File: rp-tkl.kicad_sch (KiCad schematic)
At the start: 35 parts, among them J1 USB_C_Receptacle_USB2.0, J2 SWD, J3 Conn_01x04_Female, J4 Conn_01x06_Female, SW0 SW_Push, U1 XC6206PxxxMR, U2 RP2040, U3 SRV05-4, U4 W25Q128JVS, Y1 12MHz

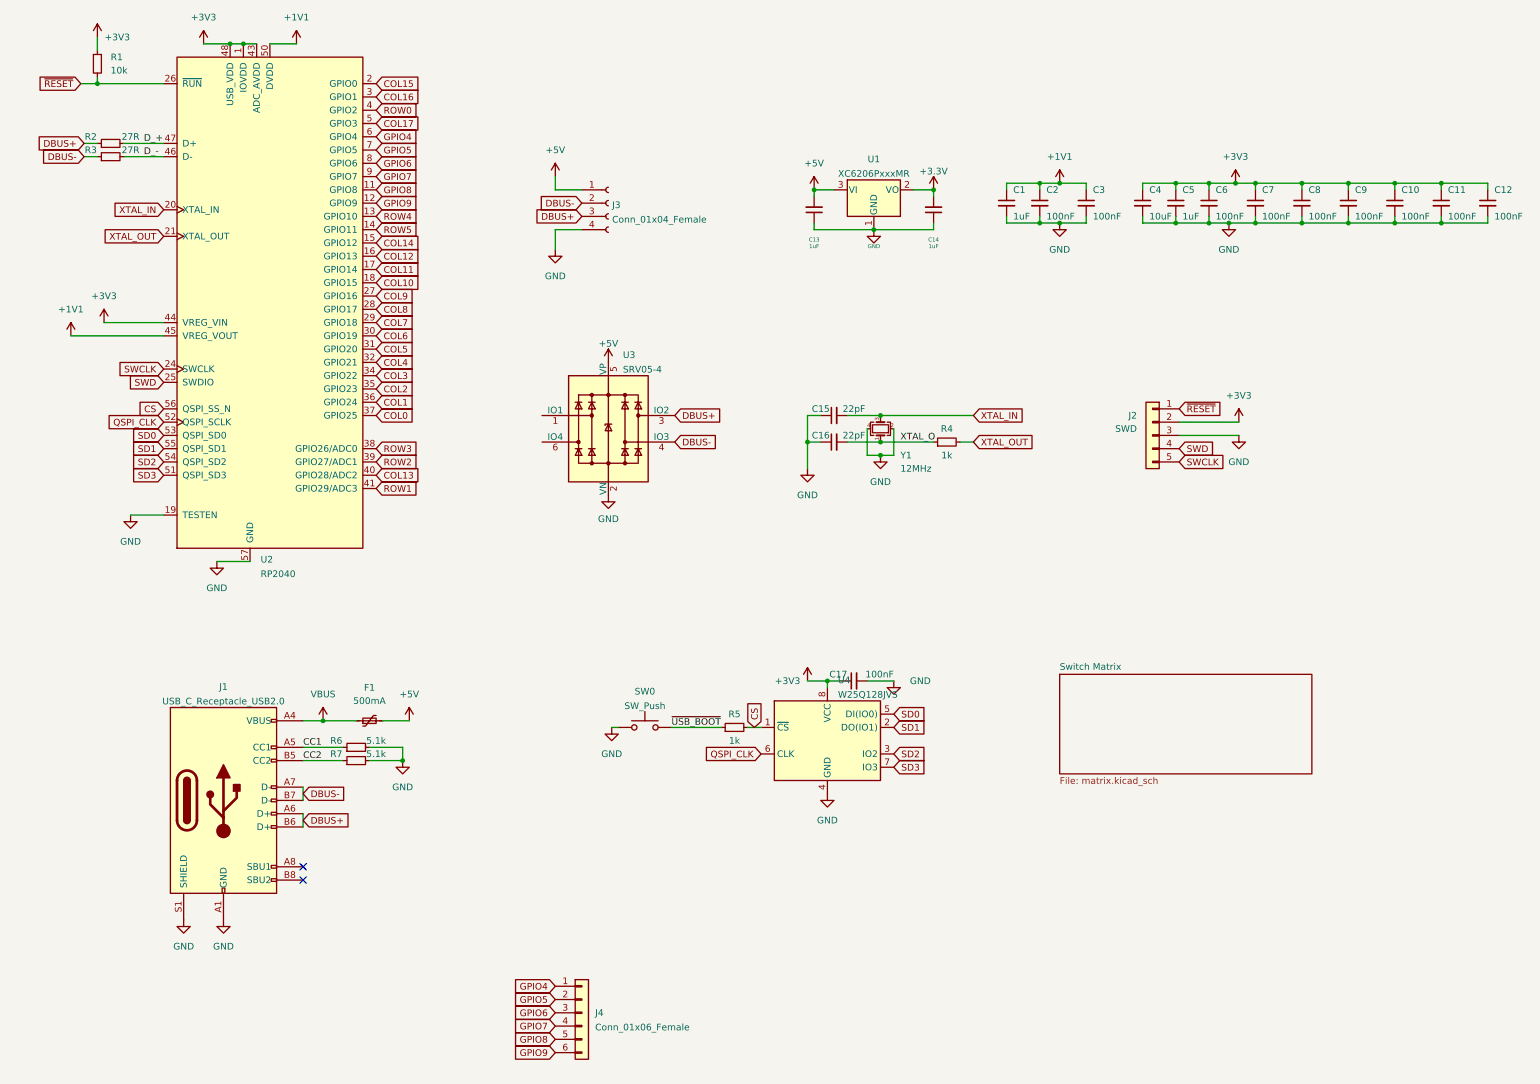
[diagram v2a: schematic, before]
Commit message: Cleaned up silkscreen and fab layers
Also adjusted some of the component descriptions/names
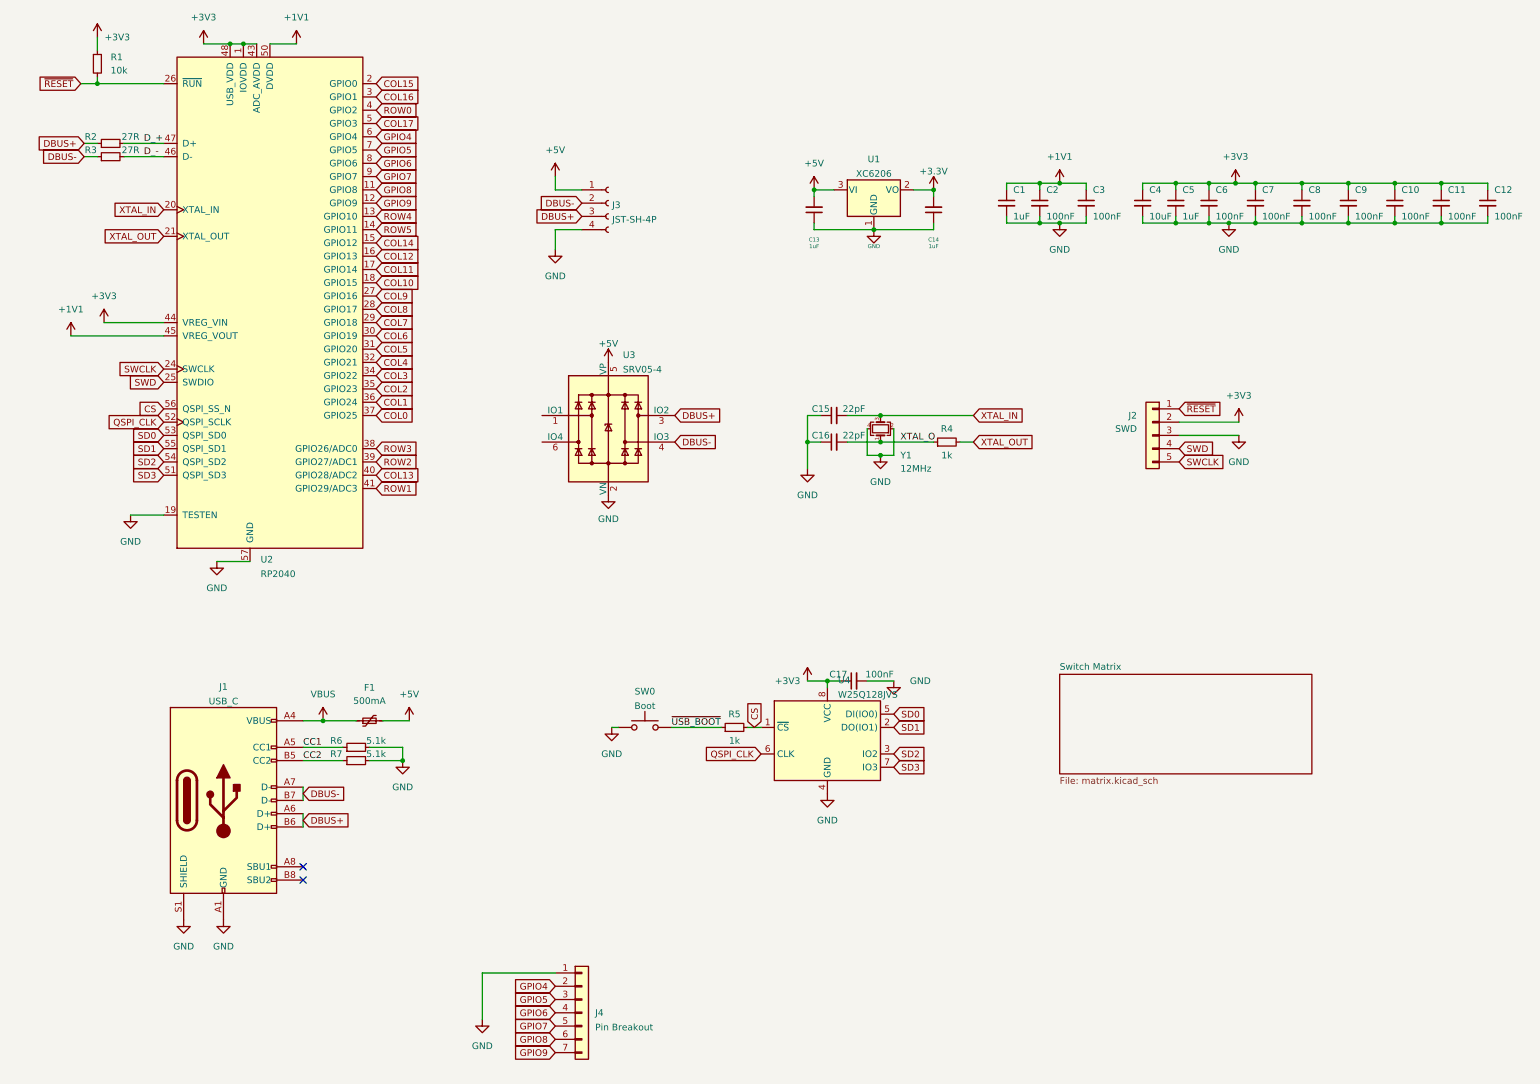
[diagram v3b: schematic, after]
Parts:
- J1: value USB_C_Receptacle_USB2.0 -> USB_C
- J3: value Conn_01x04_Female -> JST-SH-4P
- J4: value Conn_01x06_Female -> Pin Breakout; footprint Connector_PinSocket_2.54mm:PinSocket_1x06_P2.54mm_Vertical -> Connector_PinSocket_2.54mm:PinSocket_1x07_P2.54mm_Vertical; symbol Connector_Generic:Conn_01x06 -> Connector_Generic:Conn_01x07
- SW0: value SW_Push -> Boot
- U1: value XC6206PxxxMR -> XC6206
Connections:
- net GND: now also J4.1 (Pin_1)
- net GPIO4: now also J4.2 (Pin_2); no longer J4.1 (Pin_1)
- net GPIO5: now also J4.3 (Pin_3); no longer J4.2 (Pin_2)
- net GPIO6: now also J4.4 (Pin_4); no longer J4.3 (Pin_3)
- net GPIO7: now also J4.5 (Pin_5); no longer J4.4 (Pin_4)
- net GPIO8: now also J4.6 (Pin_6); no longer J4.5 (Pin_5)
- net GPIO9: now also J4.7 (Pin_7); no longer J4.6 (Pin_6)
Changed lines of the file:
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@@
+    (stroke (width 0) (type default) (color 0 0 0 0))
+  )
+  (wire (pts (xy 120.65 219.71) (xy 106.68 219.71))
     (stroke (width 0) (type default) (color 0 0 0 0))
   )
@@
   )
   (wire (pts (xy 207.01 68.58) (xy 207.01 69.85))
+    (stroke (width 0) (type default) (color 0 0 0 0))
+  )
+  (wire (pts (xy 106.68 219.71) (xy 106.68 228.6))
     (stroke (width 0) (type default) (color 0 0 0 0))
   )
@@
     (in_bom yes) (on_board yes) (fields_autoplaced)
     (property "Reference" "U1" (id 0) (at 181.61 63.9785 0))
-    (property "Value" "XC6206PxxxMR" (id 1) (at 181.61 66.7536 0))
+    (property "Value" "XC6206" (id 1) (at 181.61 66.7536 0))
     (property "Footprint" "Package_TO_SOT_SMD:SOT-23" (id 2) (at 181.61 64.135 0)
       (effects (font (size 1.27 1.27) italic) hide)
@@
     (pin "1")
   )
-  (symbol (lib_id "Connector_Generic:Conn_01x06") (at 125.73 227.33 0) (unit 1)
+  (symbol (lib_id "Connector_Generic:Conn_01x07") (at 125.73 227.33 0) (unit 1)
     (in_bom yes) (on_board yes)
     (property "Reference" "J4" (id 0) (at 128.27 227.33 0)
       (effects (font (size 1.27 1.27)) (justify left))
     )
-    (property "Value" "Conn_01x06_Female" (id 1) (at 128.27 230.1051 0)
-      (effects (font (size 1.27 1.27)) (justify left))
-    )
-    (property "Footprint" "Connector_PinSocket_2.54mm:PinSocket_1x06_P2.54mm_Vertical" (id 2) (at 125.73 227.33 0)
+    (property "Value" "Pin Breakout" (id 1) (at 128.27 230.1051 0)
+      (effects (font (size 1.27 1.27)) (justify left))
+    )
+    (property "Footprint" "Connector_PinSocket_2.54mm:PinSocket_1x07_P2.54mm_Vertical" (id 2) (at 125.73 227.33 0)
       (effects (font (size 1.27 1.27)) hide)
     )
@@
     (pin "5")
     (pin "6")
+    (pin "7")
   )
   (symbol (lib_id "Device:Crystal_GND24_Small") (at 182.88 115.57 90) (unit 1)
@@
     (in_bom yes) (on_board yes) (fields_autoplaced)
     (property "Reference" "J1" (id 0) (at 57.15 164.9435 0))
-    (property "Value" "USB_C_Receptacle_USB2.0" (id 1) (at 57.15 167.7186 0))
+    (property "Value" "USB_C" (id 1) (at 57.15 167.7186 0))
     (property "Footprint" "Connector_USB:USB_C_Receptacle_HRO_TYPE-C-31-M-12" (id 2) (at 60.96 186.69 0)
       (effects (font (size 1.27 1.27)) hide)
@@
     (pin "2")
   )
+  (symbol (lib_id "power:GND") (at 106.68 228.6 0) (unit 1)
+    (in_bom yes) (on_board yes) (fields_autoplaced)
+    (property "Reference" "#PWR0104" (id 0) (at 106.68 234.95 0)
+      (effects (font (size 1.27 1.27)) hide)
+    )
+    (property "Value" "GND" (id 1) (at 106.68 233.68 0))
+    (property "Footprint" "" (id 2) (at 106.68 228.6 0)
+      (effects (font (size 1.27 1.27)) hide)
+    )
+    (property "Datasheet" "" (id 3) (at 106.68 228.6 0)
+      (effects (font (size 1.27 1.27)) hide)
+    )
+    (pin "1")
+  )
   (symbol (lib_id "power:+5V") (at 92.71 171.45 0) (unit 1)
     (in_bom yes) (on_board yes) (fields_autoplaced)
@@
       (effects (font (size 1.27 1.27)) (justify left))
     )
-    (property "Value" "Conn_01x04_Female" (id 1) (at 131.5212 75.5266 0)
+    (property "Value" "JST-SH-4P" (id 1) (at 131.5212 75.5266 0)
       (effects (font (size 1.27 1.27)) (justify left))
     )
@@
     (in_bom no) (on_board yes) (fields_autoplaced)
     (property "Reference" "SW0" (id 0) (at 137.795 165.8325 0))
-    (property "Value" "SW_Push" (id 1) (at 137.795 168.6076 0))
+    (property "Value" "Boot" (id 1) (at 137.795 168.6076 0))
     (property "Footprint" "Connector_PinSocket_2.54mm:PinSocket_1x02_P2.54mm_Vertical" (id 2) (at 137.795 167.64 0)
       (effects (font (size 1.27 1.27)) hide)
@@
       (reference "#PWR0103") (unit 1) (value "+5V") (footprint "")
     )
+    (path "/87e21c8d-439e-4759-a401-59d374da92eb"
+      (reference "#PWR0104") (unit 1) (value "GND") (footprint "")
+    )
     (path "/29f11a32-f398-46d6-95a0-57f3be58392e"
       (reference "C1") (unit 1) (value "1uF") (footprint "Capacitor_SMD:C_0402_1005Metric")
@@
     )
     (path "/7ebbe95b-f237-4c94-ae3b-fbe07dfc9bfc"
-      (reference "J1") (unit 1) (value "USB_C_Receptacle_USB2.0") (footprint "Connector_USB:USB_C_Receptacle_HRO_TYPE-C-31-M-12")
+      (reference "J1") (unit 1) (value "USB_C") (footprint "Connector_USB:USB_C_Receptacle_HRO_TYPE-C-31-M-12")
     )
     (path "/488e1dfc-da13-4e5c-9edf-756b09e35c04"
@@
     )
     (path "/cd299587-3566-48c2-b7b0-ede206393480"
-      (reference "J3") (unit 1) (value "Conn_01x04_Female") (footprint "Connector_JST:JST_SH_SM04B-SRSS-TB_1x04-1MP_P1.00mm_Horizontal")
+      (reference "J3") (unit 1) (value "JST-SH-4P") (footprint "Connector_JST:JST_SH_SM04B-SRSS-TB_1x04-1MP_P1.00mm_Horizontal")
     )
     (path "/7e5da8d0-bec9-4daa-a9a1-871fdaa0d15e"
-      (reference "J4") (unit 1) (value "Conn_01x06_Female") (footprint "Connector_PinSocket_2.54mm:PinSocket_1x06_P2.54mm_Vertical")
+      (reference "J4") (unit 1) (value "Pin Breakout") (footprint "Connector_PinSocket_2.54mm:PinSocket_1x07_P2.54mm_Vertical")
     )
     (path "/d5f64c48-5769-4554-8a1d-d23f7b2152b1"
@@
     )
     (path "/df52ecfd-d6ac-4a2d-94d8-4402699e85fd"
-      (reference "SW0") (unit 1) (value "SW_Push") (footprint "Connector_PinSocket_2.54mm:PinSocket_1x02_P2.54mm_Vertical")
+      (reference "SW0") (unit 1) (value "Boot") (footprint "Connector_PinSocket_2.54mm:PinSocket_1x02_P2.54mm_Vertical")
     )
     (path "/0725a7ea-5a55-410a-a32c-06489f3e6998/f9175455-5dbb-4a50-9def-47a4f1e2edc0"
@@
     )
     (path "/4eb4cafb-ae77-4a3b-89a1-b20f5055f905"
-      (reference "U1") (unit 1) (value "XC6206PxxxMR") (footprint "Package_TO_SOT_SMD:SOT-23")
+      (reference "U1") (unit 1) (value "XC6206") (footprint "Package_TO_SOT_SMD:SOT-23")
     )
     (path "/6c91105f-0998-47d1-bf34-86dbf65193a4"

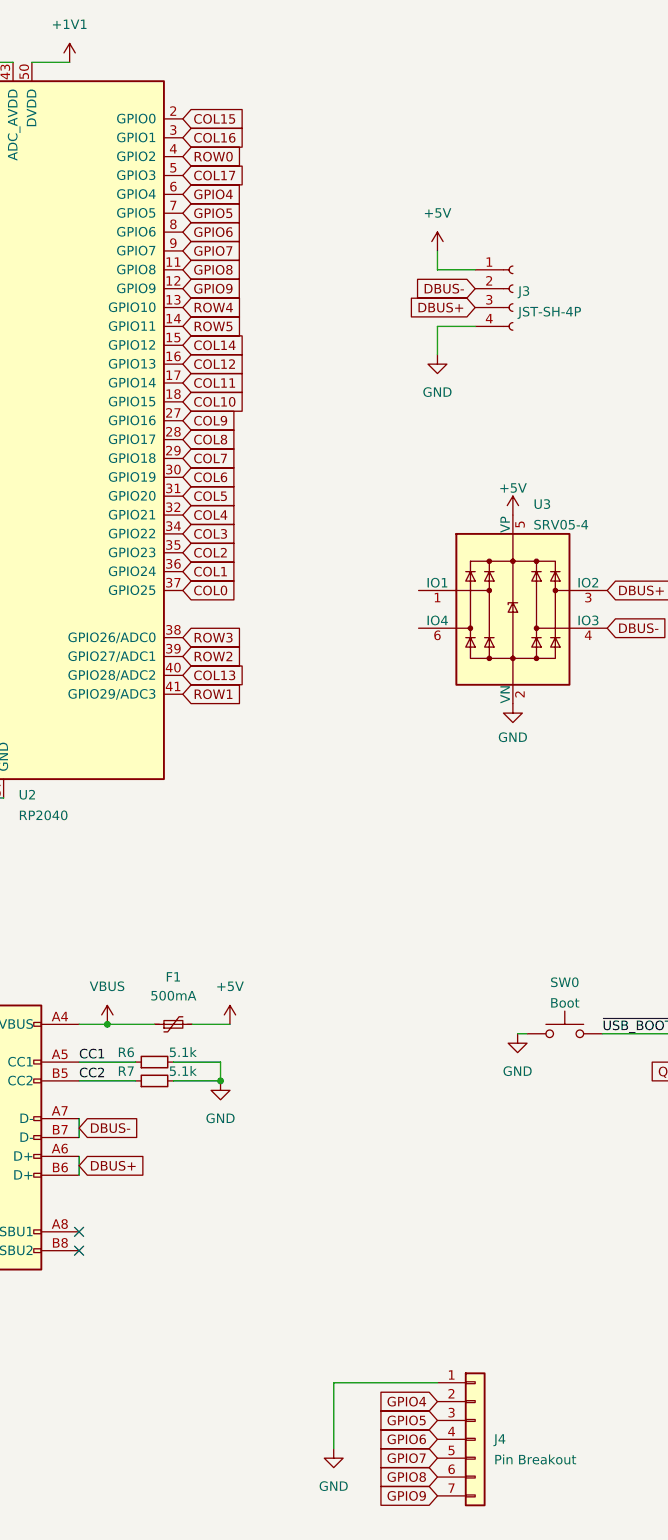
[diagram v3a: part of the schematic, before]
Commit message: [Big changes] Added flex cuts and changed switch matrix/ pinout
- Optimized switch matrix by changing how the split backspace is done. It now connects to a different row instead of creating a whole different column
- Shifted a lot of traces/pins over by one, slight retracing work around the mcu area
- Added one more pin to the unused pins header
- Added 2 simple flex cuts
- Slight shifting around of different diodes
- Added 3d model for JST and USB-C Connector
- Extended bottom of the pcb by 0.5mm to accommodate for stab holes a bit better.
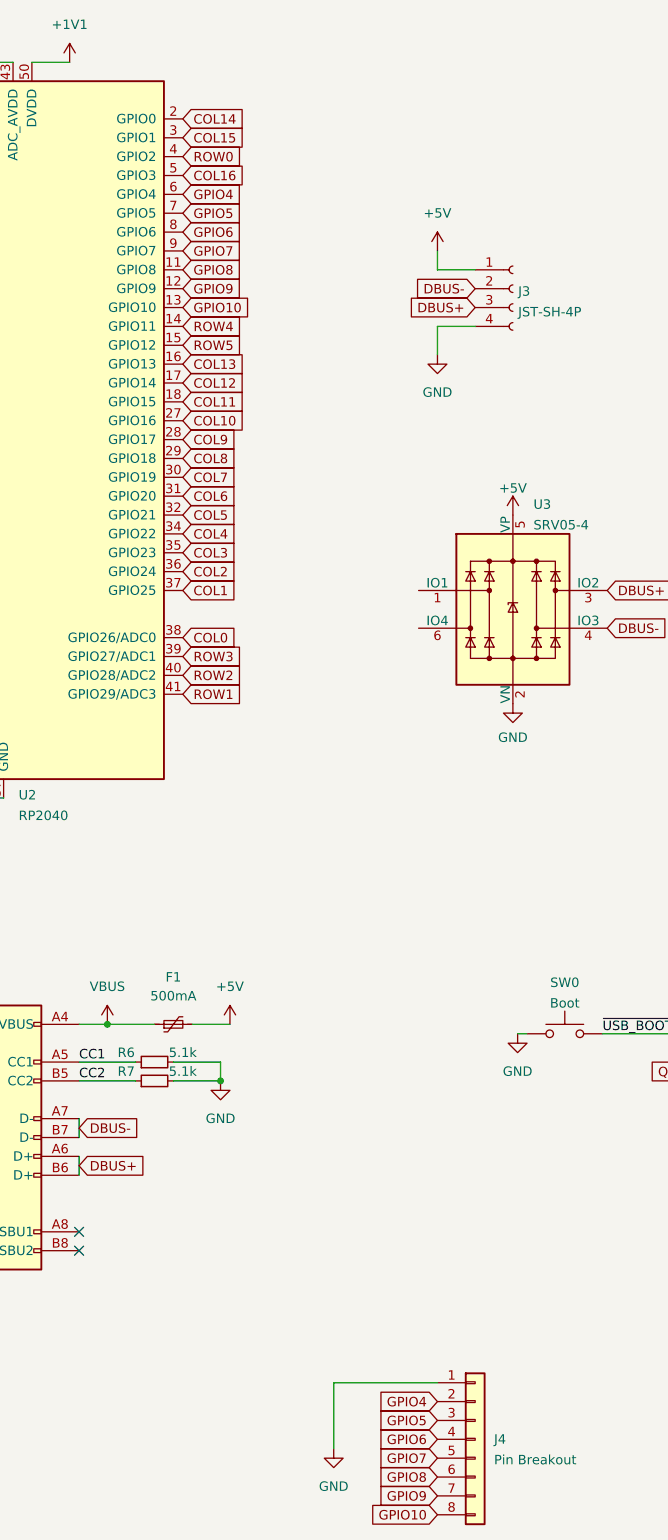
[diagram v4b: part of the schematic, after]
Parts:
- J4: footprint Connector_PinSocket_2.54mm:PinSocket_1x07_P2.54mm_Vertical -> Connector_PinSocket_2.54mm:PinSocket_1x08_P2.54mm_Vertical; symbol Connector_Generic:Conn_01x07 -> Connector_Generic:Conn_01x08
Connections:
- net COL17 is gone; now on net COL16: U2.5 (GPIO3)
- net COL0: now also U2.38 (GPIO26/ADC0); no longer U2.37 (GPIO25)
- net COL1: now also U2.37 (GPIO25); no longer U2.36 (GPIO24)
- net COL10: now also U2.27 (GPIO16); no longer U2.18 (GPIO15)
- net COL11: now also U2.18 (GPIO15); no longer U2.17 (GPIO14)
- net COL12: now also U2.17 (GPIO14); no longer U2.16 (GPIO13)
- net COL13: now also U2.16 (GPIO13); no longer U2.40 (GPIO28/ADC2)
- net COL14: now also U2.2 (GPIO0); no longer U2.15 (GPIO12)
- net COL15: now also U2.3 (GPIO1); no longer U2.2 (GPIO0)
- net COL16: no longer U2.3 (GPIO1)
- net COL2: now also U2.36 (GPIO24); no longer U2.35 (GPIO23)
- net COL3: now also U2.35 (GPIO23); no longer U2.34 (GPIO22)
- net COL4: now also U2.34 (GPIO22); no longer U2.32 (GPIO21)
- net COL5: now also U2.32 (GPIO21); no longer U2.31 (GPIO20)
- net COL6: now also U2.31 (GPIO20); no longer U2.30 (GPIO19)
- net COL7: now also U2.30 (GPIO19); no longer U2.29 (GPIO18)
- net COL8: now also U2.29 (GPIO18); no longer U2.28 (GPIO17)
- net COL9: now also U2.28 (GPIO17); no longer U2.27 (GPIO16)
- net ROW2: now also U2.40 (GPIO28/ADC2); no longer U2.39 (GPIO27/ADC1)
- net ROW3: now also U2.39 (GPIO27/ADC1); no longer U2.38 (GPIO26/ADC0)
- net ROW4: now also U2.14 (GPIO11); no longer U2.13 (GPIO10)
- net ROW5: now also U2.15 (GPIO12); no longer U2.14 (GPIO11)
- new net GPIO10: J4.8 (Pin_8), U2.13 (GPIO10)
